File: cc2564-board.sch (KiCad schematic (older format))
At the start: 65 parts, among them J1 TYPE-C-31-M-12, J2 Conn_ARM_JTAG_SWD_10, J3 Conn_Coaxial, J4 BOOT1, J5 BOOT0, J6 Conn_01x16, J7 Conn_01x16, SW1 SW_Push, U1 LD1117#33, U2 LD1117#18, U3 STM32F103C8Tx, U4 CC2564CRVMR, U5 TXB0104D, Y1 Crystal_GND24_Small, Y2 ECS-260-8-36CKM-TR, Y3 ECS-327MVATX-3-CN-TR

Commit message: Add UFL connector
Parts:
- removed C24, C25: 1uF, Capacitor_SMD:C_0603_1608Metric_Pad1.08x0.95mm_HandSolder, symbol Device:C
- removed C26, C27: 0.1uF, Capacitor_SMD:C_0603_1608Metric_Pad1.08x0.95mm_HandSolder, symbol Device:C
- removed C28, C29: 0.47uF, Capacitor_SMD:C_0603_1608Metric_Pad1.08x0.95mm_HandSolder, symbol Device:C
- added C? (x2): 0.1uF, Capacitor_SMD:C_0603_1608Metric_Pad1.08x0.95mm_HandSolder, symbol Device:C
- added J?: 1909763-1, digikey-footprints:UMCoax_Pin_1909763-1, symbol dk_Coaxial-Connectors-RF:1909763-1
- added R?: 10k, Resistor_SMD:R_0402_1005Metric_Pad0.72x0.64mm_HandSolder, symbol Device:R
- added R?: 0, symbol Device:R
- added U?: TXB0104D, Package_SO:SOIC-14_3.9x8.7mm_P1.27mm, symbol Logic_LevelTranslator:TXB0104D
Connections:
- net labels added: NSHUTDOWN, NSHUTDOWN_1V8, NSHUTD_1V8
- net labels removed: DIG_LDO_OUT, MLDO_OUT
- wire segments 212 -> 218
- no-connect marks 36 -> 40
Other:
- note added: "DNP"
- moved on the sheet: C13, C14, C15, C16, C21, C22, D2, D3, D4, J4, J5, J6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

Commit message: RF matching placeholder and filtering
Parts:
- removed J3: Conn_Coaxial, symbol Connector:Conn_Coaxial
- added AE1: Interted-F Antenna, symbol Device:Antenna
- added C26, C27: DNP, Capacitor_SMD:C_0603_1608Metric_Pad1.08x0.95mm_HandSolder, symbol Device:C
- added C28: 22pF, Capacitor_SMD:C_0603_1608Metric_Pad1.08x0.95mm_HandSolder, symbol Device:C
- added J8: Conn_01x04, Connector_PinHeader_1.27mm:PinHeader_1x04_P1.27mm_Vertical, symbol Connector_Generic:Conn_01x04
- added L2: 0ohm, Inductor_SMD:L_0402_1005Metric_Pad0.77x0.64mm_HandSolder, symbol pspice:INDUCTOR
- added R15: 0, Resistor_SMD:R_0402_1005Metric_Pad0.72x0.64mm_HandSolder, symbol Device:R
- added U8: DEA202450BT-1213C1, DEA-4_2P0X1P25, symbol DEA202450BT-1213C1:DEA202450BT-1213C1
- R16: renamed from R?; footprint (none) -> Resistor_SMD:R_0402_1005Metric_Pad0.72x0.64mm_HandSolder
- gave numbers to parts that had none: 9
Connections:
- net labels removed: BT_AUD_CLK, BT_AUD_FSYNC, BT_AUD_IN, BT_AUD_OUT, NSHUTD_1V8, PB0
- wire segments 218 -> 231
- no-connect marks 40 -> 50
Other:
- note added: "4-Wire UART Interface (H4 Protocol)\n\n> If no external battery is used in the application,\nit is highly recommended to connect VBAT externally to VDD(with 100nF decoupling cap)"
- note added: "DC blocking\nrequired for CC2564\nblock 5th harmonic?\n"
- note added: "PCB trace should have 50 ohm impedence\npi network could later be used for impedence matching\nBPF itself is ‘impedence matched’ for 50ohm in/out"
- note removed: "4-Wire UART Interface (H4 Protocol)\n\nVDD_A for ADC, don’t need precision so using same supply is fine\n> If no external battery is used in the application,\nit is highly recommended to connect VBAT externally to VDD(with 100nF decoupling cap)"
- moved on the sheet: D2, D3, D4, J3, J6, J7, R10, R16, R8, R9, U4B

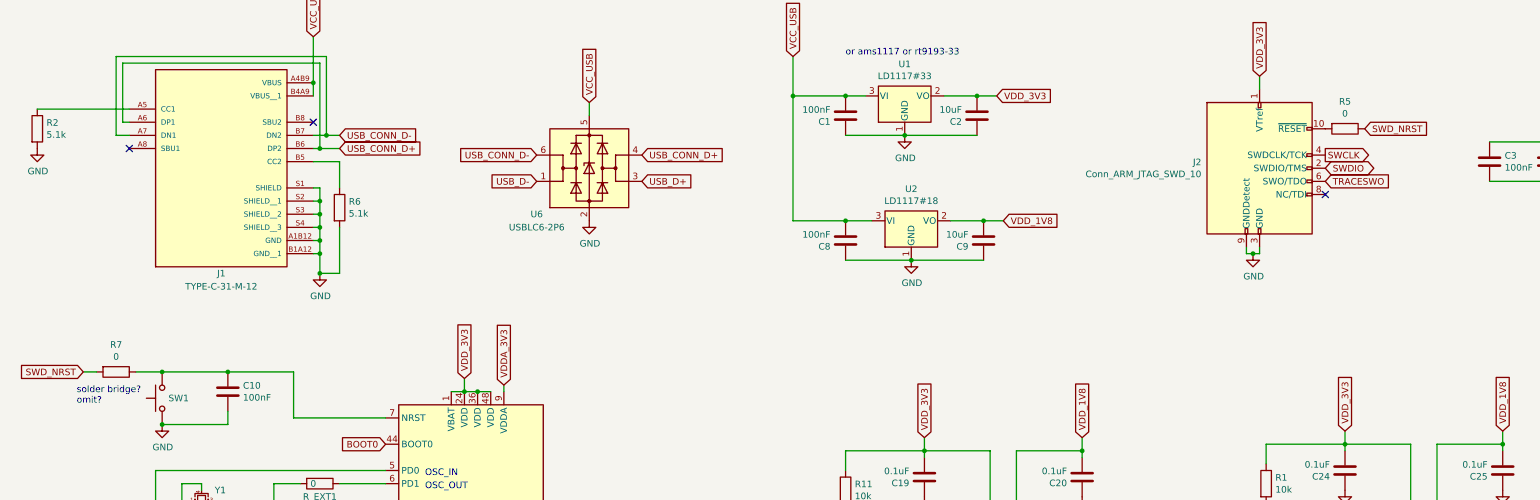
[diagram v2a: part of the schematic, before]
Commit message: Remove extra 0ohm on SWD_NRST
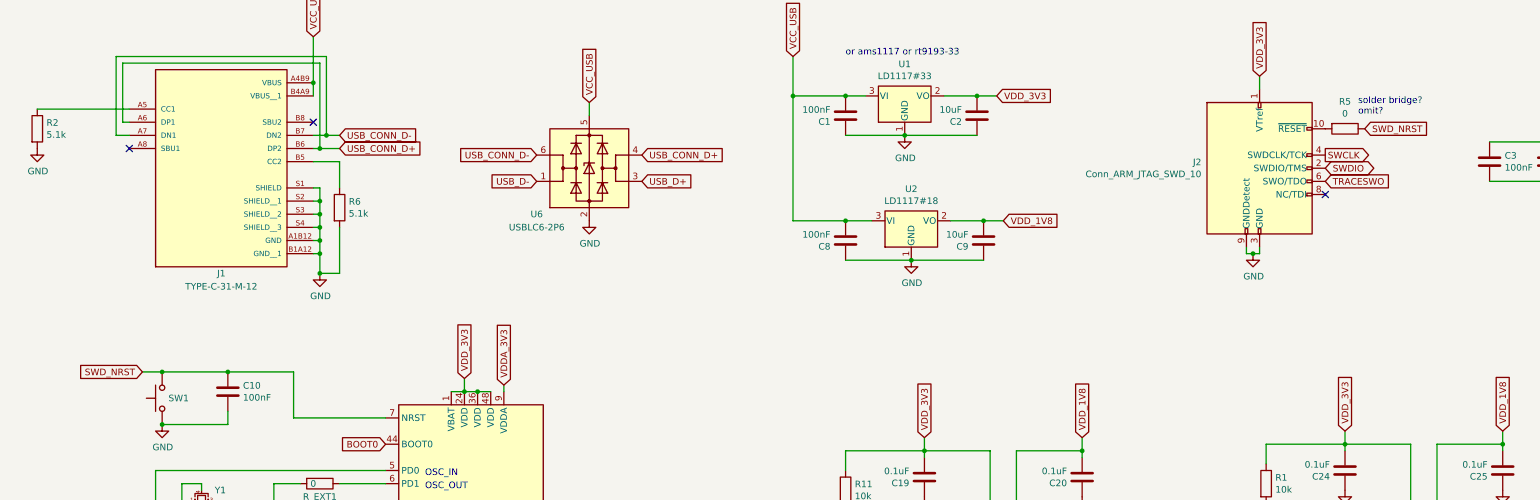
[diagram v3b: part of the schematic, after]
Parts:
- removed R7: 0, Resistor_SMD:R_0402_1005Metric_Pad0.72x0.64mm_HandSolder, symbol Device:R
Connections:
- net SWD_NRST: now also C10.1, SW1.2, U3.7 (NRST)
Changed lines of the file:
@@
 Text GLabel 10950 1750 2    50   Input ~ 0
 SWD_NRST
-Text GLabel 1200 3600 0    50   Input ~ 0
+Text GLabel 1650 3600 0    50   Input ~ 0
 SWD_NRST
 $Comp
@@
 Wire Wire Line
 	7500 2750 7000 2750
-$Comp
-L Device:R R7
-U 1 1 6004FFCD
-P 1450 3600
-F 0 "R7" V 1243 3600 50  0000 C CNN
-F 1 "0" V 1334 3600 50  0000 C CNN
-F 2 "Resistor_SMD:R_0402_1005Metric_Pad0.72x0.64mm_HandSolder" V 1380 3600 50  0001 C CNN
-F 3 "~" H 1450 3600 50  0001 C CNN
-	1    1450 3600
-	0    1    1    0
-$EndComp
-Wire Wire Line
-	1200 3600 1300 3600
-Wire Wire Line
-	1600 3600 1800 3600
 Connection ~ 1800 3600
-Text Notes 1150 3850 0    50   ~ 0
+Text Notes 10900 1650 0    50   ~ 0
 solder bridge?\nomit?\n
 Text Notes 1200 5400 0    50   ~ 0
@@
 NoConn ~ 4300 11200
 NoConn ~ 4300 11300
+Wire Wire Line
+	1650 3600 1800 3600
 $EndSCHEMATC

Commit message: Fix up a bunch of footprints
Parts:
- removed J3: 1909763-1, digikey-footprints:UMCoax_Pin_1909763-1, symbol dk_Coaxial-Connectors-RF:1909763-1
- removed Y1: Crystal_GND24_Small, symbol Device:Crystal_GND24_Small
- added J7: 1909763-1, cc2654-board-footprints:UFL-TE_1909763-1, symbol UFL-CONNECTOR:1909763-1
- added Y1: ECS-80-18-30-JGN-TR, cc2654-board-footprints:XTAL_ECS-80-18-30-JGN-TR, symbol ECS-80-18-30-JGN-TR:ECS-80-18-30-JGN-TR
- AE1: value Interted-F Antenna -> Inverted-F Antenna
- FL1: renamed from U8; footprint DEA-4_2P0X1P25 -> cc2654-board-footprints:DEA202450BT-1213C1
- SW1: footprint (none) -> cc2654-board-footprints:TL3342F160QG_TR
- U6: renamed from U5; footprint Package_SO:SOIC-14_3.9x8.7mm_P1.27mm -> cc2654-board-footprints:TXB0104D
- Y3: renamed from Y2; footprint (none) -> cc2654-board-footprints:XTAL_ECS-160-10-36-JGN-TR
- renumbered C23 to C10, C8 to C11, C9 to C12, C10 to C13, C24 to C14, C25 to C15, C19 to C16, C20 to C17, C17 to C18, C18 to C19, C26 to C20, C27 to C21, C28 to C22, C13 to C23, C14 to C24, C15 to C25, C16 to C26, C21 to C27, C22 to C28, C11 to C8, C12 to C9, D4 to D1, J6 to J3, J7 to J4, J4 to J5, J5 to J6, R2 to R1, R4 to R10, R14 to R11, R15 to R12, R16 to R13, R12 to R14, R13 to R15, R5 to R2, R6 to R3, R10 to R4, R8 to R5, R9 to R6, R1 to R7, R11 to R8, R3 to R9, U6 to U2, U2 to U3, U3 to U4, U7 to U5, U4 to U7, Y3 to Y2
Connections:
- net GND: now also J7.2 (GND), J7.3 (GND__1); no longer C20.1, FL1.3 (OUT), L2.1
- net at C18.2, U4.5 (PD0): now also Y1.1
- net at C19.2, R_EXT1.2: now also Y1.2
- net at R13.1: now also J7.1 (SIG)
- new net: C20.1, FL1.3 (OUT), L2.1
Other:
- note added: "8MHz ±20ppm 18pF 100 Ohms 2-SMD\n"
- note removed: "ECS-80-18-30-JGN-TR\n8MHz ±20ppm 18pF 100 Ohms 2-SMD\n"
- moved on the sheet: C18, C19

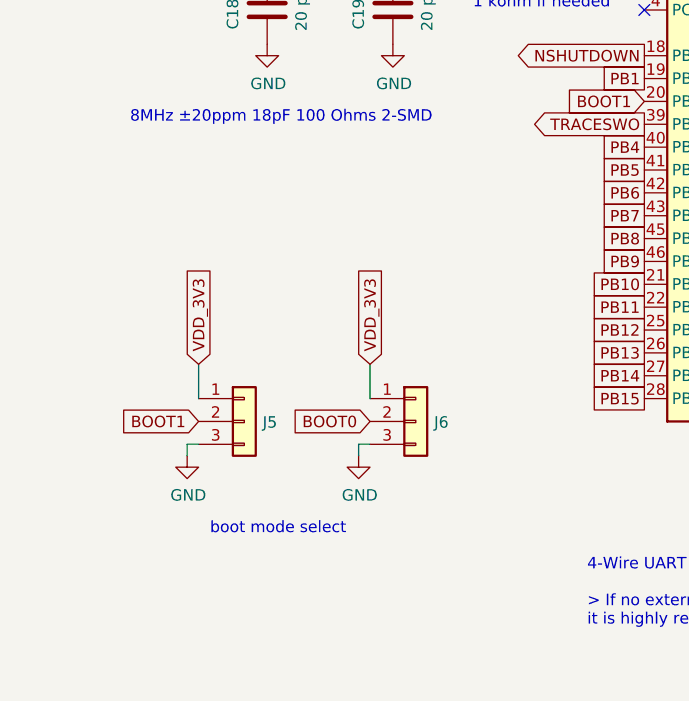
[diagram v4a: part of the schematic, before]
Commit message: One header for boot mode
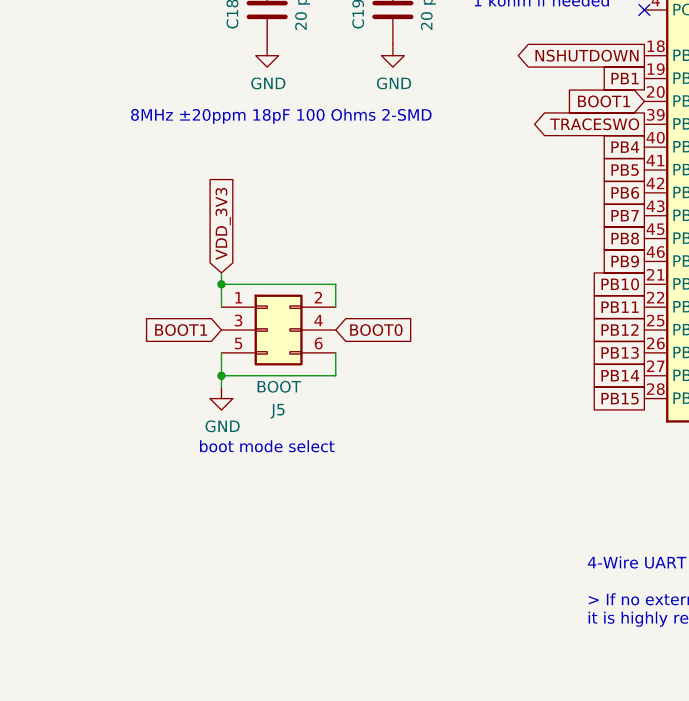
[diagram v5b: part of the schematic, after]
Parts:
- removed J5: BOOT1, Connector_PinHeader_1.27mm:PinHeader_1x03_P1.27mm_Vertical, symbol Connector_Generic:Conn_01x03
- removed J6: BOOT0, Connector_PinHeader_1.27mm:PinHeader_1x03_P1.27mm_Vertical, symbol Connector_Generic:Conn_01x03
- added J5: BOOT, Connector_PinHeader_1.27mm:PinHeader_2x03_P1.27mm_Vertical, symbol Connector_Generic:Conn_02x03_Odd_Even
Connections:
- net BOOT0: now also J5.4 (Pin_4)
- net BOOT1: now also J5.3 (Pin_3)
- net GND: now also J5.5 (Pin_5), J5.6 (Pin_6)
- net VDD_3V3: now also J5.1 (Pin_1), J5.2 (Pin_2)
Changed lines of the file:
@@
 Text Notes 3800 4400 0    50   ~ 0
 OSC_IN
-$Comp
-L Connector_Generic:Conn_01x03 J5
-U 1 1 5FF25060
-P 1750 6650
-F 0 "J5" H 1830 6646 50  0000 L CNN
-F 1 "BOOT1" H 1830 6601 50  0001 L CNN
-F 2 "Connector_PinHeader_1.27mm:PinHeader_1x03_P1.27mm_Vertical" H 1750 6650 50  0001 C CNN
-F 3 "~" H 1750 6650 50  0001 C CNN
-	1    1750 6650
-	1    0    0    -1
-$EndComp
-$Comp
-L power:GND #PWR022
-U 1 1 5FF25338
-P 1500 6800
-F 0 "#PWR022" H 1500 6550 50  0001 C CNN
-F 1 "GND" H 1505 6627 50  0000 C CNN
-F 2 "" H 1500 6800 50  0001 C CNN
-F 3 "" H 1500 6800 50  0001 C CNN
-	1    1500 6800
-	1    0    0    -1
-$EndComp
-Wire Wire Line
-	1500 6800 1500 6750
-Wire Wire Line
-	1500 6750 1550 6750
-Text GLabel 1550 6400 1    50   Input ~ 0
+Text GLabel 1650 6000 1    50   Input ~ 0
 VDD_3V3
-Wire Wire Line
-	1550 6400 1550 6550
-Text GLabel 1550 6650 0    50   Input ~ 0
+Text GLabel 1650 6250 0    50   Input ~ 0
 BOOT1
-$Comp
-L Connector_Generic:Conn_01x03 J6
-U 1 1 5FF2D2DA
-P 2500 6650
-F 0 "J6" H 2580 6646 50  0000 L CNN
-F 1 "BOOT0" H 2580 6601 50  0001 L CNN
-F 2 "Connector_PinHeader_1.27mm:PinHeader_1x03_P1.27mm_Vertical" H 2500 6650 50  0001 C CNN
-F 3 "~" H 2500 6650 50  0001 C CNN
-	1    2500 6650
-	1    0    0    -1
-$EndComp
-$Comp
-L power:GND #PWR023
-U 1 1 5FF2D2F8
-P 2250 6800
-F 0 "#PWR023" H 2250 6550 50  0001 C CNN
-F 1 "GND" H 2255 6627 50  0000 C CNN
-F 2 "" H 2250 6800 50  0001 C CNN
-F 3 "" H 2250 6800 50  0001 C CNN
-	1    2250 6800
-	1    0    0    -1
-$EndComp
-Wire Wire Line
-	2250 6800 2250 6750
-Wire Wire Line
-	2250 6750 2300 6750
-Text GLabel 2300 6400 1    50   Input ~ 0
-VDD_3V3
-Wire Wire Line
-	2300 6400 2300 6550
-Text GLabel 2300 6650 0    50   Input ~ 0
-BOOT0
-Text Notes 1600 7150 0    50   ~ 0
+Text Notes 1550 6800 0    50   ~ 0
 boot mode select
 Wire Wire Line
@@
 Wire Wire Line
 	9500 8950 9500 9100
+$Comp
+L Connector_Generic:Conn_02x03_Odd_Even J5
+U 1 1 61711DEB
+P 1850 6250
+F 0 "J5" H 1900 5900 50  0000 C CNN
+F 1 "BOOT" H 1900 6000 50  0000 C CNN
+F 2 "Connector_PinHeader_1.27mm:PinHeader_2x03_P1.27mm_Vertical" H 1850 6250 50  0001 C CNN
+F 3 "~" H 1850 6250 50  0001 C CNN
+	1    1850 6250
+	1    0    0    -1
+$EndComp
+Wire Wire Line
+	1650 6150 1650 6050
+Wire Wire Line
+	1650 6050 2150 6050
+Wire Wire Line
+	2150 6050 2150 6150
+Connection ~ 1650 6050
+Wire Wire Line
+	1650 6050 1650 6000
+Wire Wire Line
+	1650 6350 1650 6450
+Wire Wire Line
+	1650 6450 2150 6450
+Wire Wire Line
+	2150 6450 2150 6350
+$Comp
+L power:GND #PWR0101
+U 1 1 6175C9AC
+P 1650 6500
+F 0 "#PWR0101" H 1650 6250 50  0001 C CNN
+F 1 "GND" H 1655 6327 50  0000 C CNN
+F 2 "" H 1650 6500 50  0001 C CNN
+F 3 "" H 1650 6500 50  0001 C CNN
+	1    1650 6500
+	1    0    0    -1
+$EndComp
+Text GLabel 2150 6250 2    50   Input ~ 0
+BOOT0
+Wire Wire Line
+	1650 6500 1650 6450
+Connection ~ 1650 6450
 $EndSCHEMATC
